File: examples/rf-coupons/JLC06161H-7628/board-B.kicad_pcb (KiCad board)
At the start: 6 copper layers, 134 x 189 mm, 87 parts, among them X1 TestPoint_PTH, X10 TestPoint_PTH, X11 TestPoint_PTH, X12 TestPoint_PTH, X13 TestPoint_PTH, X14 TestPoint_PTH, X15 TestPoint_PTH, X16 TestPoint_PTH, X17 TestPoint_PTH, X18 TestPoint_PTH, X19 TestPoint_PTH, X2 TestPoint_PTH, X20 TestPoint_PTH, X21 TestPoint_PTH, X22 TestPoint_PTH, X23 TestPoint_PTH, X24 TestPoint_PTH, X25 TestPoint_PTH, X26 TestPoint_PTH, X27 TestPoint_PTH, X28 TestPoint_PTH, X29 TestPoint_PTH, X3 TestPoint_PTH, X30 TestPoint_PTH, X31 TestPoint_PTH, X32 TestPoint_PTH, X33 TestPoint_PTH, X34 TestPoint_PTH, X35 TestPoint_PTH, X36 TestPoint_PTH, X37 TestPoint_PTH, X38 TestPoint_PTH, X39 TestPoint_PTH, X4 TestPoint_PTH, X40 TestPoint_PTH, X41 TestPoint_PTH, X42 TestPoint_PTH, X43 TestPoint_PTH, X44 TestPoint_PTH, X45 TestPoint_PTH, X46 TestPoint_PTH, X47 TestPoint_PTH, X48 TestPoint_PTH, X49 TestPoint_PTH, X5 TestPoint_PTH, X50 TestPoint_PTH, X51 TestPoint_PTH, X52 TestPoint_PTH, X55 Microsection, X56 Anchor, X6 TestPoint_PTH, X7 TestPoint_PTH, X8 TestPoint_PTH, X9 TestPoint_PTH

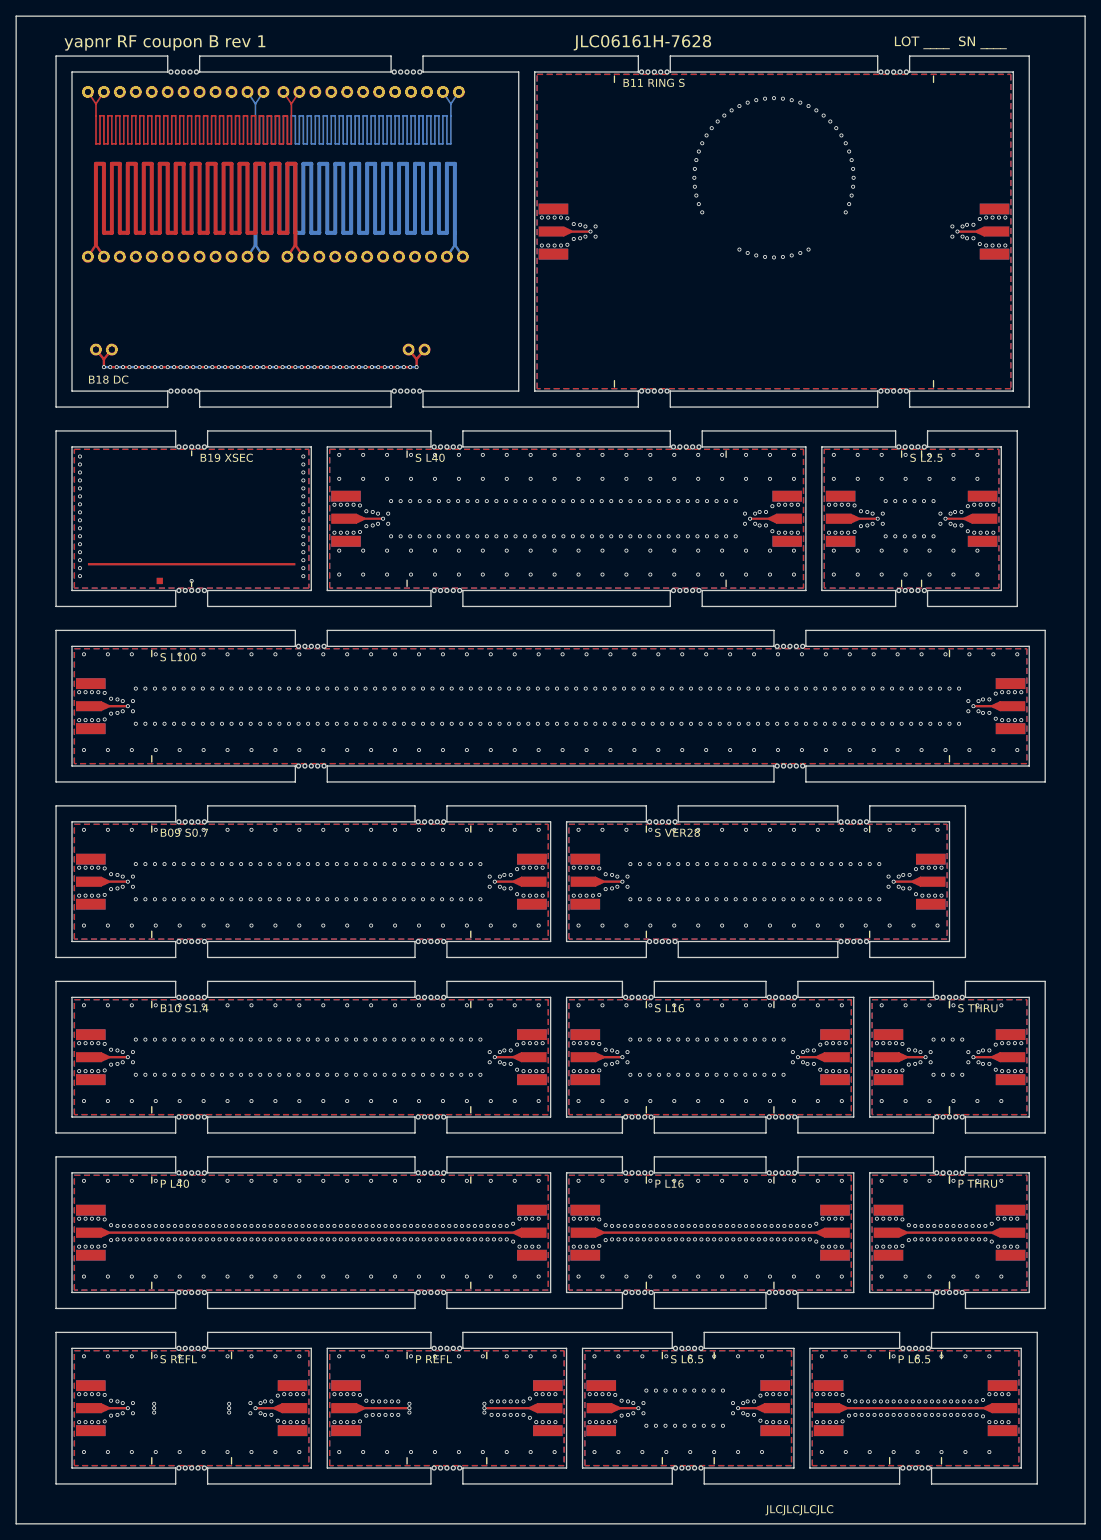
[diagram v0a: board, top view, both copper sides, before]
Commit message: RF coupons: stick ids on every label, 5 mm mouse-bite tabs, fab notes (#32)
Boards (regenerated; KiCad 10.0.6 DRC: 0 violations, 0 unconnected):
- The TRL-set sticks were labelled "P L40" with no stick id. That
  covered the whole TRL set of both boards, including board B's P tie
  set. The session file names need the id (A-03_A05-P-L40_r1.s2p), and
  design 5.5 asks for it. Every label now starts with its id. A label
  too long for a 20 mm thru ends 0.5 mm from the far edge. Labels now
  sit 1.6-2.6 mm from the long edge, below the reference-plane ticks
  (0.5-1.3 mm). The second tick of the 2.5 and 6.5 mm lines used to
  cross the text.
- Mouse-bite tabs widen from 4 mm to 5 mm, with six 0.5 mm bites at
  0.8 mm pitch. JLC's capabilities page (read 2026-10-02) asks for at
  least 5 mm on a tab with mouse bites.

Fab notes:
- They list M (0.348 mm) and say that no width or gap of any test
  structure may be changed.
- The edge clearance moves from "unverified" to checked: JLC asks for
  0.2 mm on routed edges; the zones keep 0.30 mm and DRC checks 0.25 mm.

Other changes:
- JLC06161H-7628 L4-L6 and JLC06161H-2116C L4-L6 are marked verified
  against jlcpcb.com/impedance (read 2026-10-02, and main's
  yapnr/fab/data/stackups). The values are unchanged.
- The expected-file headers no longer repeat the id.
- test_catalog checks that every label carries its id, fits its stick
  and clears the ticks.

Co-Authored-By: Claude Opus 5.5 <noreply@anthropic.com>
Claude-Session: https://claude.ai/code/session_01NY8rMuBH8hTFjkoZyuqNZ7
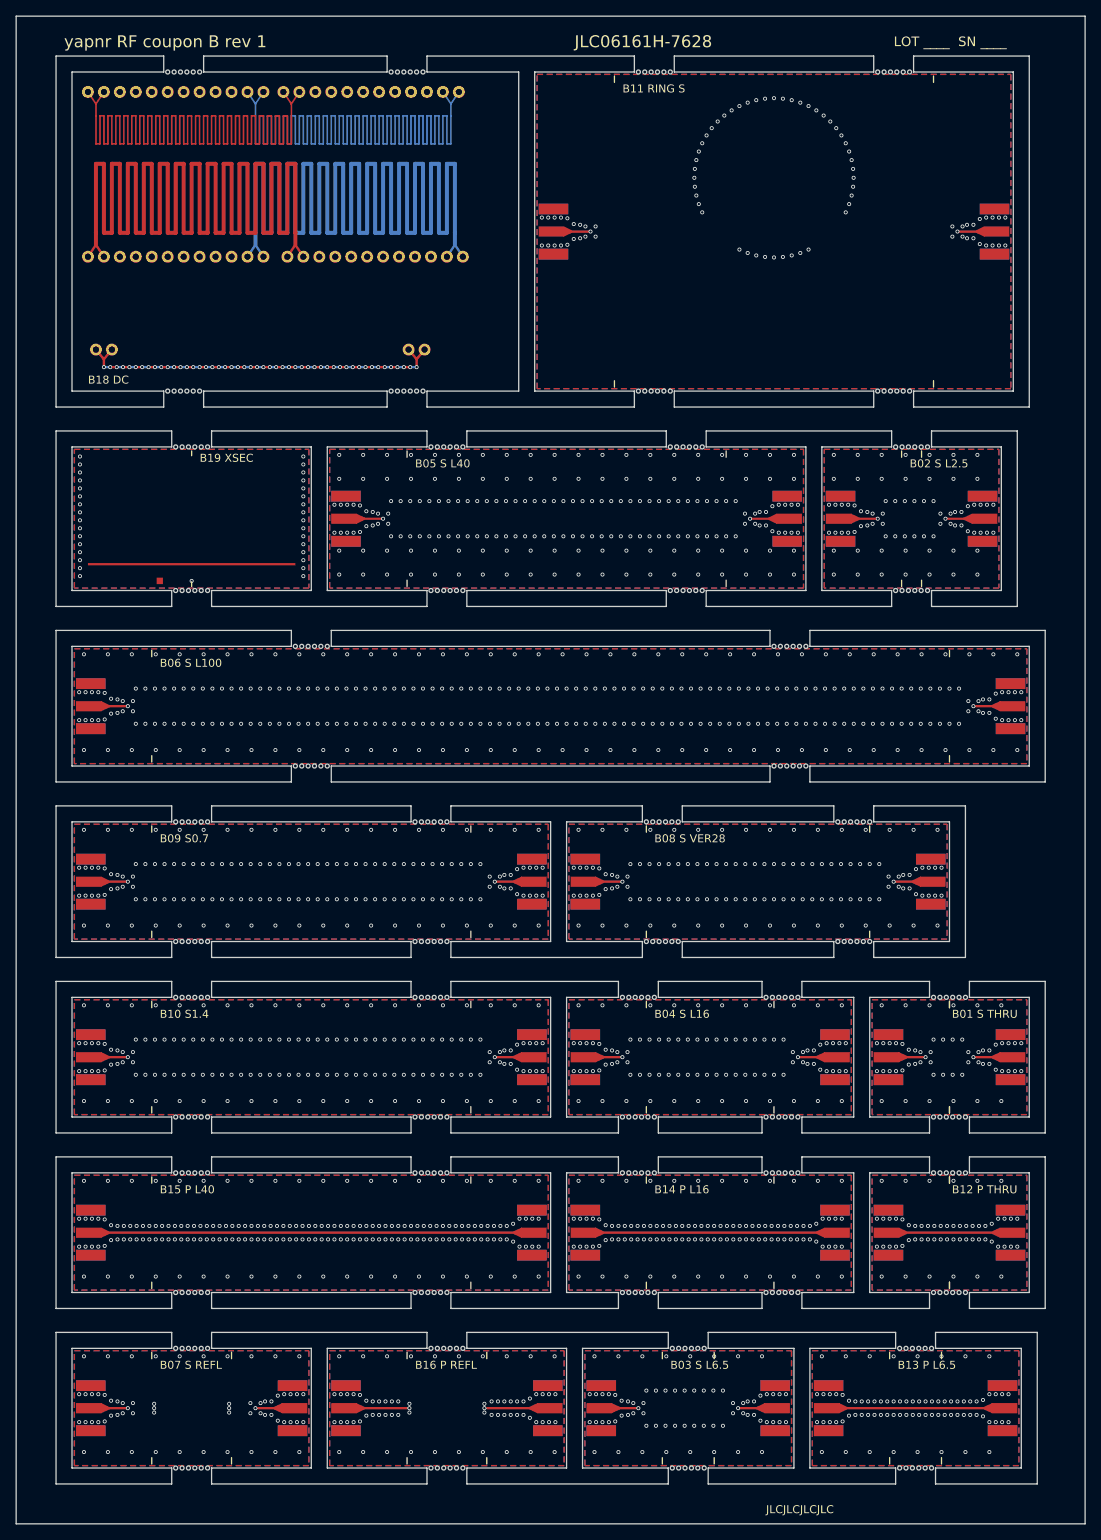
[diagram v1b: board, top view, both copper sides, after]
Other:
- outline, holes or cut-outs redrawn
- board text added: "B01 S THRU"
- board text added: "B02 S L2.5"
- board text added: "B03 S L6.5"
- board text added: "B04 S L16"
- board text added: "B05 S L40"
- board text added: "B06 S L100"
- board text added: "B07 S REFL"
- board text added: "B08 S VER28"
- board text added: "B12 P THRU"
- board text added: "B13 P L6.5"
- board text added: "B14 P L16"
- board text added: "B15 P L40"
- board text added: "B16 P REFL"
- board text removed: "P L16"
- board text removed: "P L40"
- board text removed: "P L6.5"
- board text removed: "P REFL"
- board text removed: "P THRU"
- board text removed: "S L100"
- board text removed: "S L16"
- board text removed: "S L2.5"
- board text removed: "S L40"
- board text removed: "S L6.5"
- board text removed: "S REFL"
- board text removed: "S THRU"
- board text removed: "S VER28"
